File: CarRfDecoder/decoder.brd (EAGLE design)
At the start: 98.7 x 80 mm, 49 parts, among them T1 BC847, T2 BC847, T3 IRLML6402, U1 ATMEGA32U4TQFP-44, U2 RFM69CW, U3 MCP73831, U6 MIC5219 3.3V

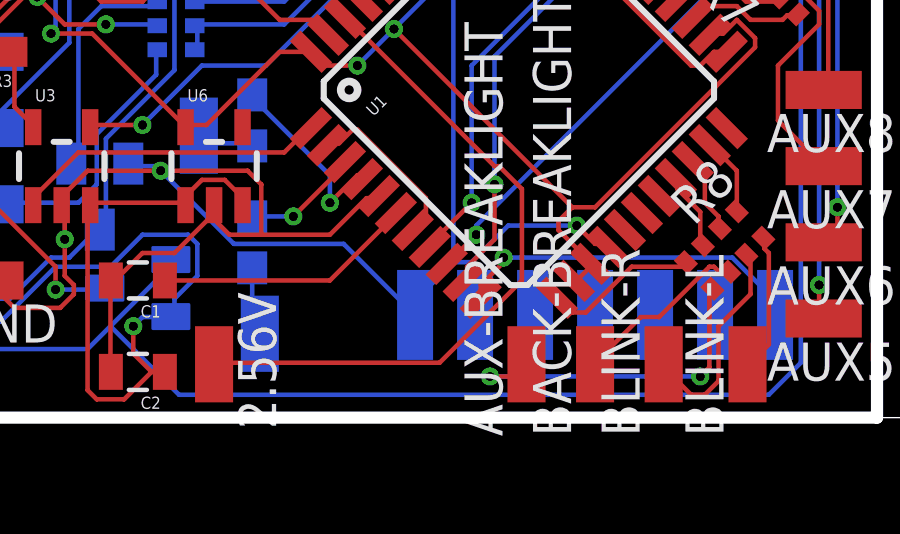
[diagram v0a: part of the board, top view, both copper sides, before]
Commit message: added pin D3 to the board and changed the D11.
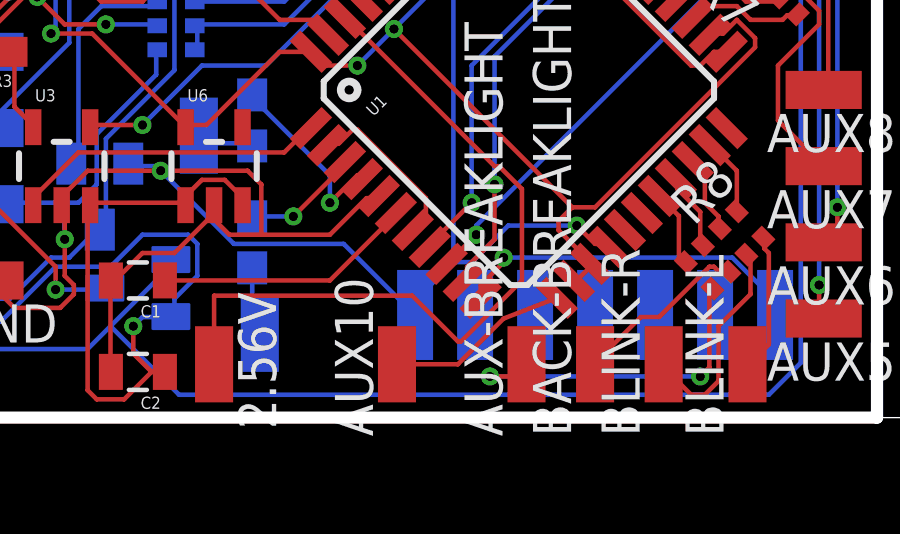
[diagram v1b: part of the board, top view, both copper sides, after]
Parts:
- added AUX10: (no value), wirepad:SMD1,27-2,54
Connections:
- net D11: now also AUX10.1; no longer R8.4
- net D3: now also R8.4
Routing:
- net D3: track 0.00 -> 2.71 mm
- net AREF: track 22.7 -> 25.4 mm
- net D11: track 5.19 -> 6.10 mm
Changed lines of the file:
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@@
 <layer number="23" name="tOrigins" color="15" fill="1" visible="yes" active="yes"/>
 <layer number="24" name="bOrigins" color="15" fill="1" visible="yes" active="yes"/>
-<layer number="25" name="tNames" color="7" fill="1" visible="no" active="yes"/>
-<layer number="26" name="bNames" color="7" fill="1" visible="no" active="yes"/>
+<layer number="25" name="tNames" color="7" fill="1" visible="yes" active="yes"/>
+<layer number="26" name="bNames" color="7" fill="1" visible="yes" active="yes"/>
 <layer number="27" name="tValues" color="7" fill="1" visible="no" active="yes"/>
 <layer number="28" name="bValues" color="7" fill="1" visible="no" active="yes"/>
@@
 <element name="USBV-" library="wirepad" package="SMD1,27-2,54" value="" x="3.302" y="7.112" rot="MR90"/>
 <element name="U2" library="SparkFun-RF" package="RFM69CW-XXXS2" value="RFM69CW" x="23.622" y="10.922" rot="MR270"/>
+<element name="AUX10" library="wirepad" package="SMD1,27-2,54" value="" x="17.018" y="1.778"/>
 </elements>
 <signals>
@@
 <wire x1="21.1836" y1="7.62" x2="20.4216" y2="8.382" width="0.1524" layer="1"/>
 <wire x1="21.1836" y1="4.572" x2="21.1836" y2="7.62" width="0.1524" layer="1"/>
-<wire x1="18.4404" y1="1.8288" x2="21.1836" y2="4.572" width="0.1524" layer="1"/>
-<wire x1="10.9728" y1="1.8288" x2="18.4404" y2="1.8288" width="0.1524" layer="1"/>
 <wire x1="15.3924" y1="13.2588" x2="15.283721875" y2="13.3261625" width="0.1524" layer="1"/>
 <wire x1="10.9728" y1="1.8288" x2="10.922" y2="1.778" width="0.1524" layer="1"/>
+<wire x1="10.9728" y1="1.8288" x2="10.922" y2="1.8796" width="0.1524" layer="1"/>
+<wire x1="10.922" y1="1.8796" x2="10.922" y2="4.064" width="0.1524" layer="1"/>
+<wire x1="10.922" y1="4.064" x2="17.526" y2="4.064" width="0.1524" layer="1"/>
+<wire x1="17.526" y1="4.064" x2="19.05" y2="2.54" width="0.1524" layer="1"/>
+<wire x1="19.05" y1="2.54" x2="19.1516" y2="2.54" width="0.1524" layer="1"/>
+<wire x1="19.1516" y1="2.54" x2="21.1836" y2="4.572" width="0.1524" layer="1"/>
 </signal>
 <signal name="N$7">
@@
 <signal name="D3">
 <contactref element="U1" pad="18"/>
+<contactref element="R8" pad="4"/>
+<wire x1="26.649528125" y1="5.1814125" x2="26.416" y2="5.1814125" width="0.1524" layer="1"/>
+<wire x1="26.416" y1="5.1814125" x2="26.416" y2="6.71936875" width="0.1524" layer="1"/>
+<wire x1="26.416" y1="6.71936875" x2="25.748903125" y2="7.386465625" width="0.1524" layer="1"/>
 </signal>
 <signal name="D4">
@@
 <signal name="D11">
 <contactref element="U1" pad="12"/>
-<contactref element="R8" pad="4"/>
-<wire x1="24.8412" y1="5.0292" x2="26.5176" y2="5.0292" width="0.1524" layer="1"/>
-<wire x1="23.3172" y1="3.5052" x2="24.8412" y2="5.0292" width="0.1524" layer="1"/>
-<wire x1="22.86" y1="3.5052" x2="23.3172" y2="3.5052" width="0.1524" layer="1"/>
-<wire x1="22.4028" y1="3.9624" x2="22.86" y2="3.5052" width="0.1524" layer="1"/>
-<wire x1="26.5176" y1="5.0292" x2="26.649528125" y2="5.1814125" width="0.1524" layer="1"/>
-<wire x1="22.4028" y1="3.9624" x2="22.354790625" y2="3.992353125" width="0.1524" layer="1"/>
+<contactref element="AUX10" pad="1"/>
+<wire x1="17.018" y1="1.778" x2="19.05" y2="1.778" width="0.1524" layer="1"/>
+<wire x1="19.05" y1="1.778" x2="20.574" y2="3.302" width="0.1524" layer="1"/>
+<wire x1="20.574" y1="3.302" x2="22.354790625" y2="3.992353125" width="0.1524" layer="1"/>
 </signal>
 <signal name="D12">

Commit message: final board decoder
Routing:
- net N$29: vias 0 -> 1
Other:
- board text added: "3.3v"
- board text added: "USBD+"
- board text added: "USBD-"
- board text added: "V+"
- board text added: "gnd"
- board text added: "hss"
- board text added: "miso"
- board text added: "mosi"
- board text added: "rst"
- board text added: "sck"

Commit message: car decoder
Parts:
- renumbered AUX-BREAKLIGHT to ABRKLIGHT, BACK-BREAKLIGHT to BBRKLIGHT
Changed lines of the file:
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@@
 <layer number="20" name="Dimension" color="15" fill="1" visible="yes" active="yes"/>
 <layer number="21" name="tPlace" color="7" fill="1" visible="yes" active="yes"/>
-<layer number="22" name="bPlace" color="7" fill="1" visible="no" active="yes"/>
+<layer number="22" name="bPlace" color="7" fill="1" visible="yes" active="yes"/>
 <layer number="23" name="tOrigins" color="15" fill="1" visible="no" active="yes"/>
 <layer number="24" name="bOrigins" color="15" fill="1" visible="no" active="yes"/>
@@
 <element name="2.56V" library="wirepad" package="SMD1,27-2,54" value="" x="10.922" y="1.778" rot="R180"/>
 <element name="3.3V" library="wirepad" package="SMD1,27-2,54" value="" x="3.302" y="16.002" rot="R90"/>
-<element name="AUX-BREAKLIGHT" library="wirepad" package="SMD1,27-2,54" value="" x="21.336" y="1.778"/>
+<element name="ABRKLIGHT" library="wirepad" package="SMD1,27-2,54" value="" x="21.336" y="1.778"/>
 <element name="AUX1" library="wirepad" package="SMD1,27-2,54" value="" x="23.622" y="21.082" rot="R180"/>
 <element name="AUX2" library="wirepad" package="SMD1,27-2,54" value="" x="27.432" y="21.082" rot="R180"/>
@@
 <element name="AUX8" library="wirepad" package="SMD1,27-2,54" value="" x="31.242" y="10.922" rot="R90"/>
 <element name="AUX9" library="wirepad" package="SMD1,27-2,54" value="" x="18.542" y="21.082" rot="R180"/>
-<element name="BACK-BREAKLIGHT" library="wirepad" package="SMD1,27-2,54" value="" x="23.622" y="1.778"/>
+<element name="BBRKLIGHT" library="wirepad" package="SMD1,27-2,54" value="" x="23.622" y="1.778"/>
 <element name="BLINK-L" library="wirepad" package="SMD1,27-2,54" value="" x="28.702" y="1.778"/>
 <element name="BLINK-R" library="wirepad" package="SMD1,27-2,54" value="" x="25.908" y="1.778"/>
@@
 <signal name="N$18">
 <contactref element="R8" pad="6"/>
-<contactref element="BACK-BREAKLIGHT" pad="1"/>
+<contactref element="BBRKLIGHT" pad="1"/>
 <wire x1="27.7368" y1="4.8768" x2="28.0416" y2="4.8768" width="0.1524" layer="1"/>
 <wire x1="27.5844" y1="5.0292" x2="27.7368" y2="4.8768" width="0.1524" layer="1"/>
@@
 <signal name="N$20">
 <contactref element="R8" pad="5"/>
-<contactref element="AUX-BREAKLIGHT" pad="1"/>
+<contactref element="ABRKLIGHT" pad="1"/>
 <wire x1="27.432" y1="1.6764" x2="27.432" y2="4.2672" width="0.1524" layer="1"/>
 <wire x1="27.1272" y1="1.3716" x2="27.432" y2="1.6764" width="0.1524" layer="1"/>

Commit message: changes in the design
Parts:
- added C5, C6: 22pF, SparkFun-Capacitors:0805
- added R12: 2K, SparkFun-Resistors:0603-RES
- added RST, XTAL, XTAL1: (no value), wirepad:SMD1,27-2,54
- moved AUX5 15.5 mm to (31.8, 18.8)
- moved AUX6 11.2 mm to (31.8, 17.0)
- moved ABRKLIGHT 10.7 mm to (31.8, 4.32), turned to 90 degrees
- moved BBRKLIGHT 9.33 mm to (31.8, 6.35), turned to 90 degrees
- moved BLINK-L 9.16 mm to (31.8, 10.4), turned to 90 degrees
- moved BLINK-R 8.82 mm to (31.8, 8.38), turned to 90 degrees
- moved R3 4.44 mm to (7.11, 14.5)
- moved AUX7 4.10 mm to (31.8, 12.4)
- moved AUX8 3.34 mm to (31.8, 14.2)
- moved AUX4 2.59 mm to (30.7, 21.1)
- moved 2.56V 2.09 mm to (13.0, 1.27)
- moved C2 2.09 mm to (7.87, 3.56)
- moved U6 2.05 mm to (9.91, 10.2)
- moved T2 2.03 mm to (7.11, 9.40)
- moved 10K 1.78 mm to (7.11, 16.5)
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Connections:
- new net N$3: C5.2, U1.17, XTAL.1
- new net N$4: C6.2, U1.16, XTAL1.1
- new net N$5: R12.1, RST.1, U1.13
- net GND: now also C5.1, C6.1
- net VCC: now also R12.2; no longer U1.13
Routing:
- net N$14: track 78.1 -> 30.2 mm, vias 4 -> 0
- net N$9: track 31.1 -> 13.3 mm, vias 3 -> 1
- net GND: track 140.1 -> 153.8 mm, vias 6 -> 5
- net VCC: track 58.9 -> 70.7 mm, vias 5 -> 2
- net AREF: track 25.4 -> 13.6 mm, vias 0 -> 2
- net N$3: track 0.00 -> 11.2 mm
- net N$25: track 14.6 -> 3.69 mm, vias 2 -> 0
- net A4: track 7.02 -> 16.5 mm, vias 1 -> 3
- net N$26: track 11.2 -> 2.67 mm, vias 2 -> 0
- net N$4: track 0.00 -> 8.33 mm
- net N$15: track 19.8 -> 27.3 mm, vias 3 -> 2
- net N$20: track 11.6 -> 4.37 mm, vias 2 -> 0
- net D11: track 6.10 -> 12.3 mm, vias 0 -> 2
- net SS: track 23.2 -> 17.5 mm
- net N$5: track 0.00 -> 5.51 mm
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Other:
- outline, holes or cut-outs redrawn

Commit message: some improvement on the boards.
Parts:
- turned XTAL to 180 degrees
- turned XTAL1 to 180 degrees
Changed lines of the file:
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@@
 <layer number="23" name="tOrigins" color="15" fill="1" visible="yes" active="yes"/>
 <layer number="24" name="bOrigins" color="15" fill="1" visible="yes" active="yes"/>
-<layer number="25" name="tNames" color="7" fill="1" visible="no" active="yes"/>
+<layer number="25" name="tNames" color="7" fill="1" visible="yes" active="yes"/>
 <layer number="26" name="bNames" color="7" fill="1" visible="yes" active="yes"/>
 <layer number="27" name="tValues" color="7" fill="1" visible="no" active="yes"/>
@@
 <text x="30.226" y="20.32" size="0.6096" layer="122" rot="MR0">hss</text>
 <text x="28.194" y="20.32" size="0.6096" layer="122" rot="MR0">sck</text>
-<text x="30.988" y="0.762" size="0.6096" layer="122" rot="MR0">miso</text>
+<text x="30.734" y="1.27" size="0.6096" layer="122" rot="MR0">miso</text>
 <text x="26.162" y="20.32" size="0.6096" layer="122" rot="MR0">mosi</text>
 <text x="22.352" y="20.32" size="0.6096" layer="122" rot="MR0">gnd</text>
@@
 <element name="U2" library="SparkFun-RF" package="RFM69CW-XXXS2" value="RFM69CW" x="23.622" y="10.922" rot="MR270"/>
 <element name="AUX10" library="wirepad" package="SMD1,27-2,54" value="" x="17.018" y="1.27"/>
-<element name="XTAL" library="wirepad" package="SMD1,27-2,54" value="" x="25.654" y="1.27"/>
-<element name="XTAL1" library="wirepad" package="SMD1,27-2,54" value="" x="23.876" y="1.27"/>
+<element name="XTAL" library="wirepad" package="SMD1,27-2,54" value="" x="25.654" y="1.27" rot="R180"/>
+<element name="XTAL1" library="wirepad" package="SMD1,27-2,54" value="" x="23.876" y="1.27" rot="R180"/>
 <element name="C5" library="SparkFun-Capacitors" package="0805" value="22pF" x="29.718" y="1.778" rot="R90"/>
 <element name="C6" library="SparkFun-Capacitors" package="0805" value="22pF" x="27.686" y="1.778" rot="R90"/>

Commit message: Ready boards.
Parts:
- added VJ, VJ1: (no value), wirepad:SMD1,27-2,54
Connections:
- new net N$31: U2.2, VJ.1
- net VCC: now also VJ1.1; no longer U2.2
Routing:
- net VCC: track 70.7 -> 94.7 mm, vias 2 -> 6
- net A4: track 16.5 -> 5.83 mm, vias 3 -> 1
- net N$31: track 0.00 -> 6.34 mm
- net N$14: track 30.2 -> 24.3 mm
- net D-: track 3.87 -> 9.52 mm
- net SCK: track 17.0 -> 21.4 mm
- net N$15: track 27.3 -> 24.2 mm, vias 2 -> 3
- net N$9: track 13.3 -> 10.5 mm
- net SS: track 17.5 -> 20.1 mm
- net A3: track 19.4 -> 17.3 mm
- net N$10: track 54.8 -> 53.0 mm, vias 3 -> 2
- net MISO: track 13.0 -> 11.6 mm
- net D11: track 12.3 -> 11.3 mm, vias 2 -> 0
- net A0: track 25.9 -> 24.8 mm
- net N$2: track 6.29 -> 7.28 mm
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
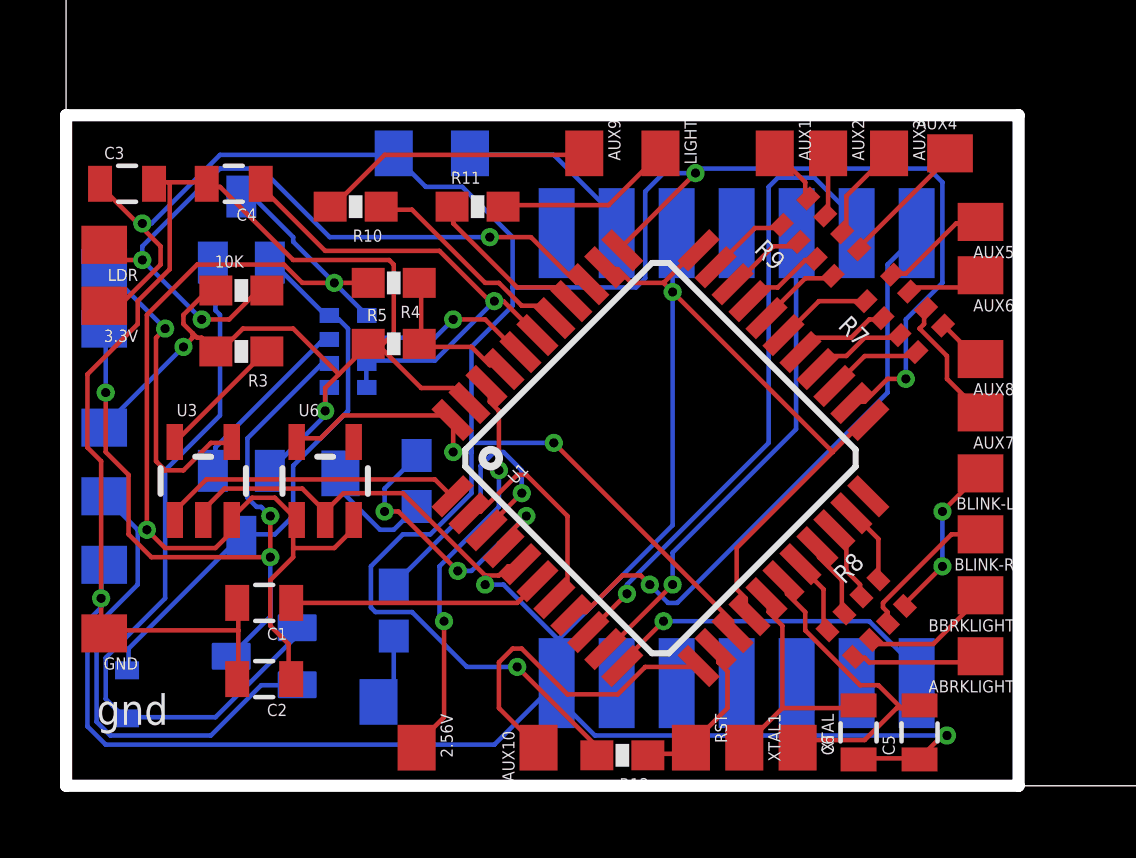
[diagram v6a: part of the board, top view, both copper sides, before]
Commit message: Fix connection to the rf module and add a 16mhz crystal
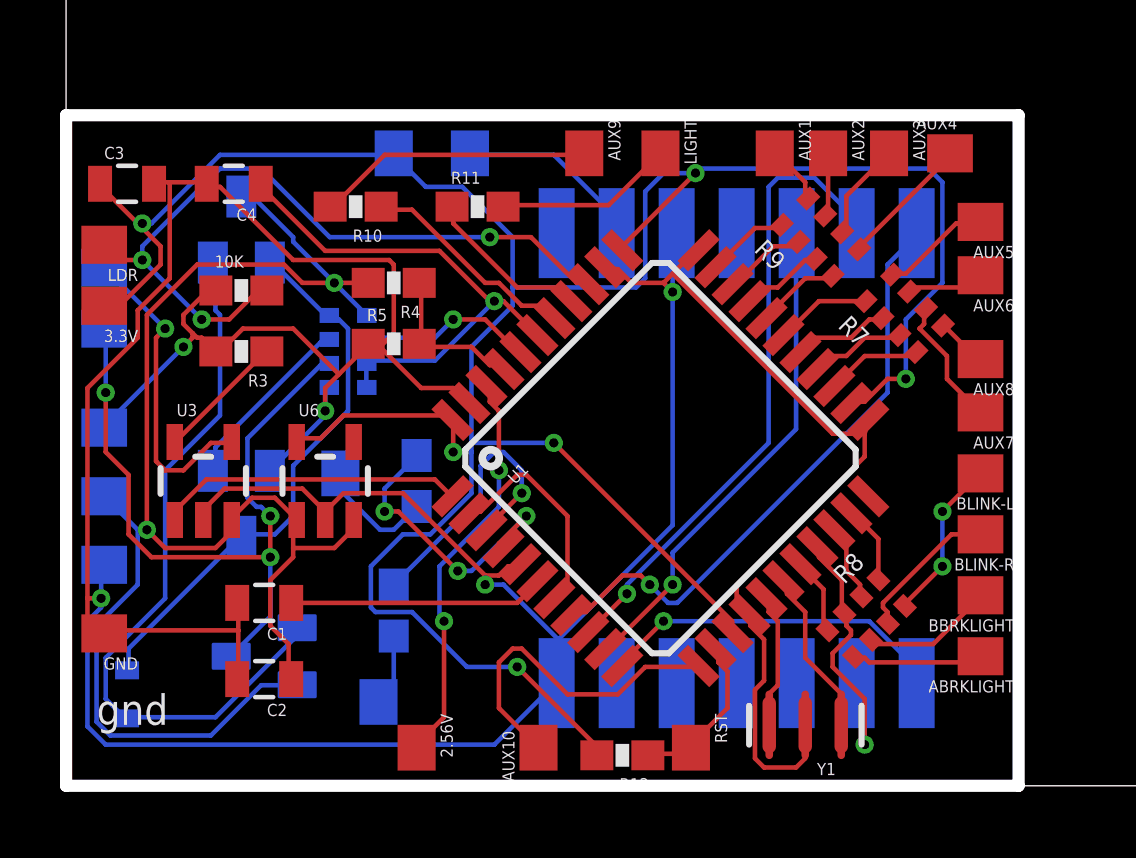
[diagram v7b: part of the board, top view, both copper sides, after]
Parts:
- removed C5, C6: 22pF, SparkFun-Capacitors:0805
- removed XTAL, XTAL1: (no value), wirepad:SMD1,27-2,54
- added Y1: 16MHZ, SparkFun-FreqCtrl:RESONATOR-SMD
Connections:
- net D2: now also U2.9
- net GND: now also Y1.2; no longer C5.1, C6.1
- net N$3: now also Y1.1; no longer C5.2, XTAL.1
- net N$4: now also Y1.3; no longer C6.2, XTAL1.1
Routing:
- net GND: track 154.6 -> 146.0 mm, vias 6 -> 5
- net D2: track 2.61 -> 9.93 mm, vias 0 -> 1
- net N$3: track 10.9 -> 5.59 mm
- net N$4: track 8.33 -> 4.54 mm
